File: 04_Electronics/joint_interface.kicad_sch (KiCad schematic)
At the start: 44 parts, among them J1 5V INPUT, J2 MCU 3V3 I/O, J3 ENCODER 3V3, J4 NC LIMIT, J5 3V3 DRIVE I/O, J6 RS485 BUS, J7 E-STOP AUX NC, U1 AP2112K-3.3, U2 LTC2850IS8

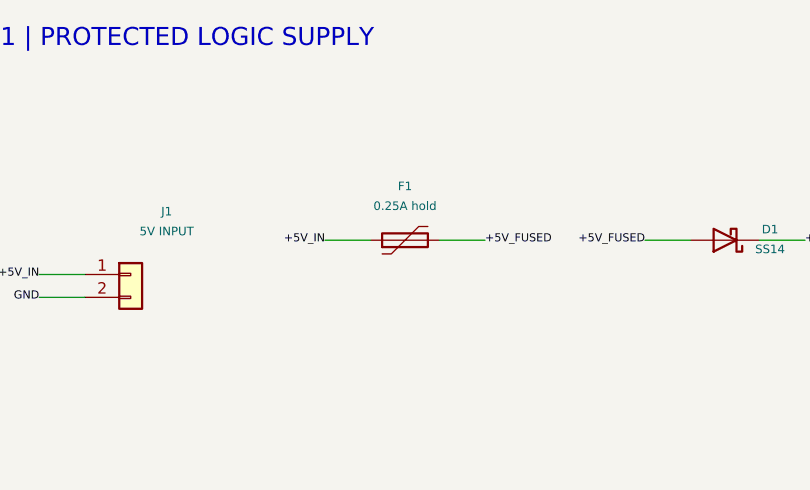
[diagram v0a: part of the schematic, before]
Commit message: Review engineering models and polish ASTER-6 component access
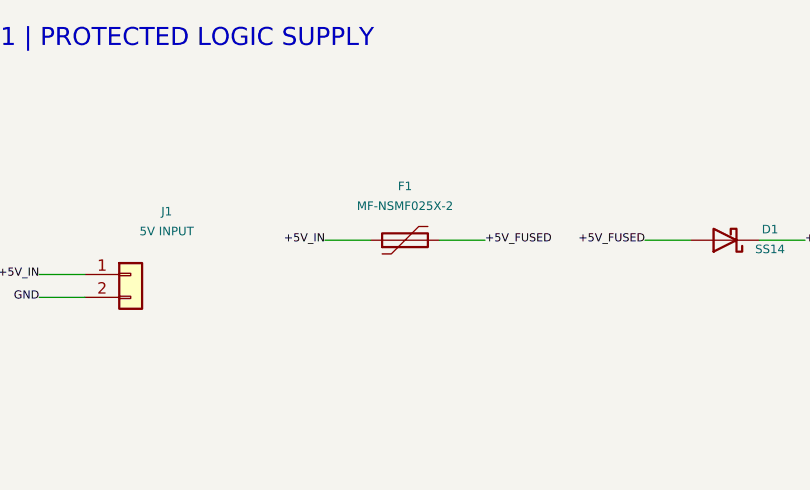
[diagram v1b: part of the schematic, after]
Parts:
- F1: value 0.25A hold -> MF-NSMF025X-2; footprint Fuse:Fuse_1206_3216Metric -> ASTER_Interface:PTC_Bourns_MF-NSMF025X_1206

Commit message: Rename the complete digital engineering project to INDRBT
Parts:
- F1: footprint ASTER_Interface:PTC_Bourns_MF-NSMF025X_1206 -> INDRBT_Interface:PTC_Bourns_MF-NSMF025X_1206
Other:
- title: ASTER-6 | Joint / Sensor Interface -> INDRBT | Joint / Sensor Interface
